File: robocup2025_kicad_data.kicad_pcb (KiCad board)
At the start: 2 copper layers, 11 parts, among them U1 RASPBERRY_PI_4B_4GB, U2 ESP32-DEVKITC-32E

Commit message: robocup2025_kicad_data.kicad_pcb,robocup2025_kicad_data.kicad_sch: Commit
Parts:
- U1: footprint robo:MODULE_RASPBERRY_PI_4B_4GB -> robo:raspberrypi5 small
- moved U1 19.0 mm to (136.1, 86.4)

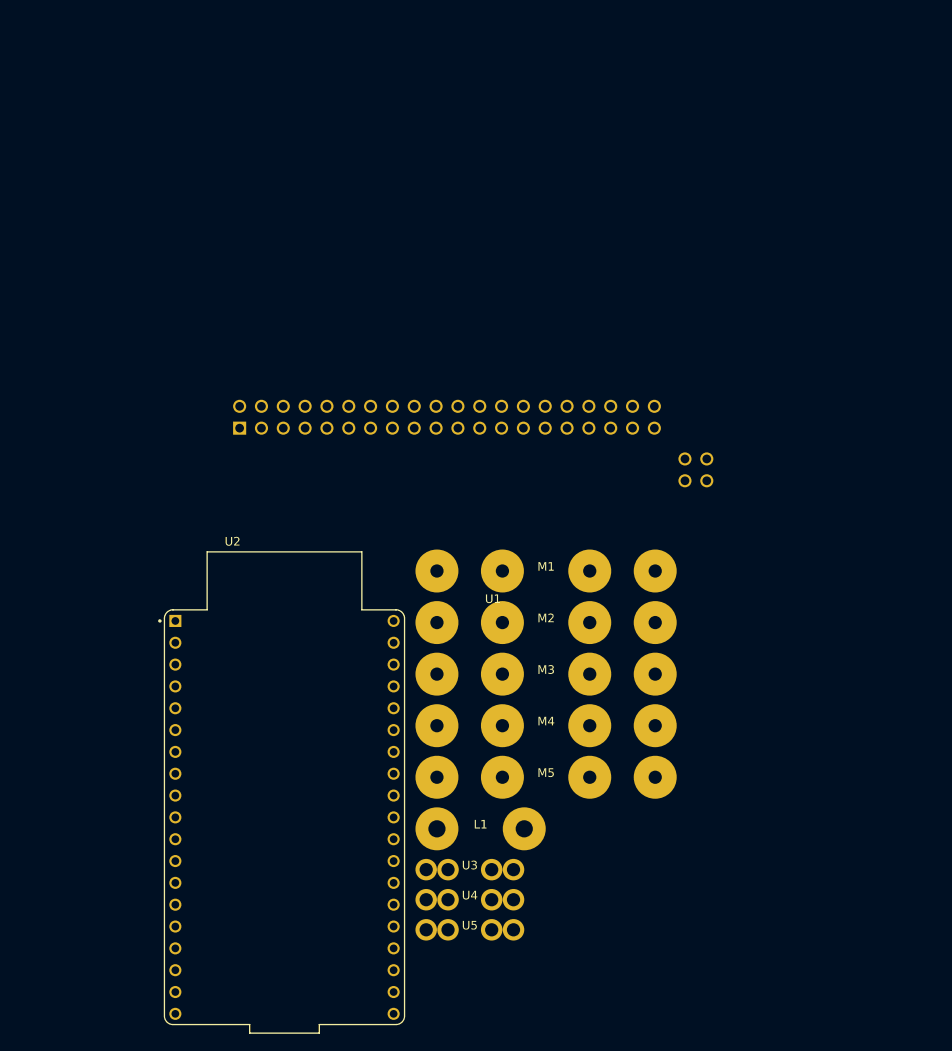
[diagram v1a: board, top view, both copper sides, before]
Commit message: robocup2025_kicad_data.kicad_pcb,robocup2025_kicad_data.kicad_prl: Replaced footprint, created cut layer
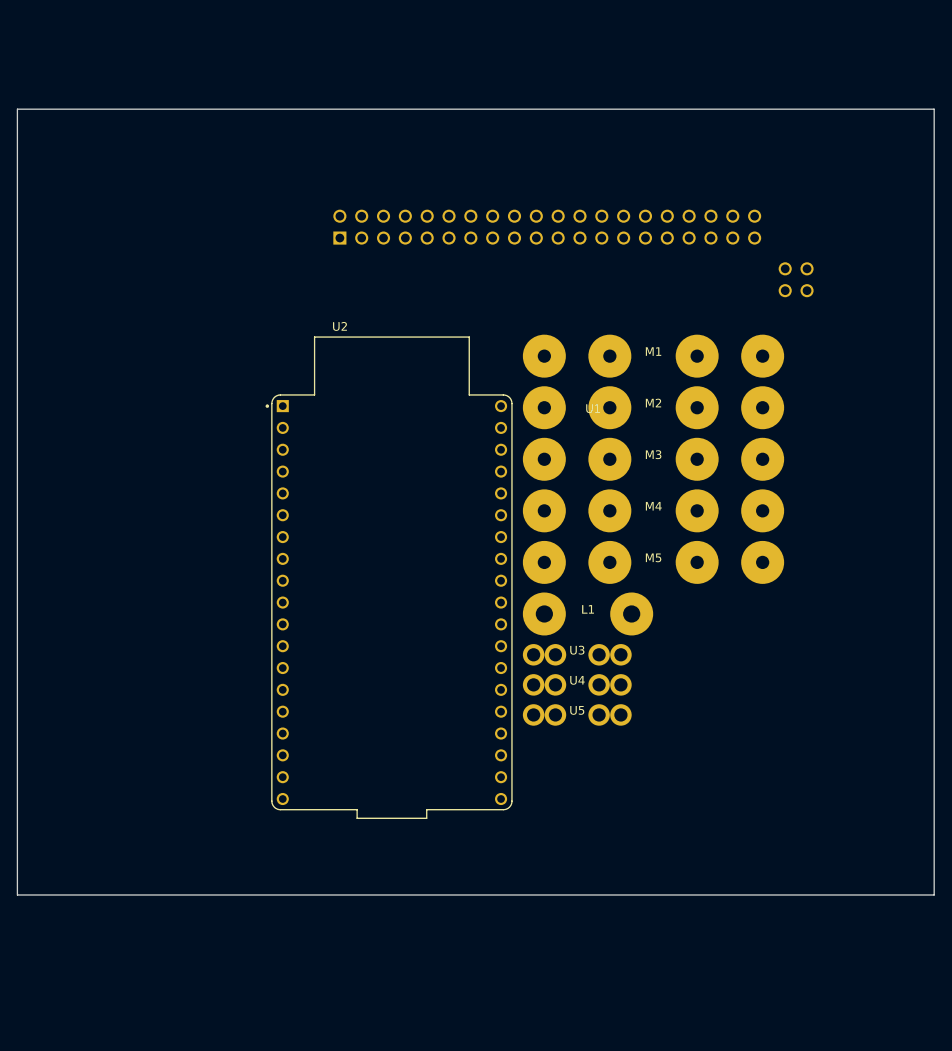
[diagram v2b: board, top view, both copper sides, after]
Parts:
- moved U2 28.0 mm to (124.9, 105.6)
- moved L1 28.0 mm to (147.7, 107.0)
- moved M1 28.0 mm to (155.3, 77.0)
- moved M2 28.0 mm to (155.3, 83.0)
- moved M3 28.0 mm to (155.3, 89.0)
- moved M4 28.0 mm to (155.3, 95.0)
- moved M5 28.0 mm to (155.3, 101.0)
- moved U3 28.0 mm to (146.4, 111.8)
- moved U4 28.0 mm to (146.4, 115.2)
- moved U5 28.0 mm to (146.4, 118.8)
- moved U1 25.0 mm to (147.8, 64.3)
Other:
- board outline added: 106.7 x 91.4 mm
- copper layers 2 -> 4

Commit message: robocup2025_kicad_data.kicad_pcb,robocup2025_kicad_data.kicad_prl robocup2025_kicad_data.kicad_pro: Set settings
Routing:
- added copper zone on B.Cu, net GND
- added copper zone on F.Cu, net LiPo+
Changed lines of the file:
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@@
 		(layer "Edge.Cuts")
+	)
+	(zone
+		(net 1)
+		(net_name "LiPo+")
+		(layer "F.Cu")
+		(hatch edge 0.5)
+		(connect_pads
+			(clearance 0.5)
+		)
+		(min_thickness 0.25)
+		(filled_areas_thickness no)
+		(fill yes
+			(thermal_gap 0.5)
+			(thermal_bridge_width 0.5)
+		)
+		(polygon
+			(pts
+				(xy 81.28 48.26) (xy 187.96 48.26) (xy 187.96 139.7) (xy 81.28 139.7)
+			)
+		)
+	)
+	(zone
+		(net 2)
+		(net_name "GND")
+		(layer "B.Cu")
+		(hatch edge 0.5)
+		(priority 1)
+		(connect_pads
+			(clearance 0.5)
+		)
+		(min_thickness 0.25)
+		(filled_areas_thickness no)
+		(fill yes
+			(thermal_gap 0.5)
+			(thermal_bridge_width 0.5)
+		)
+		(polygon
+			(pts
+				(xy 187.96 139.7) (xy 81.28 139.7) (xy 81.28 48.26) (xy 187.96 48.26)
+			)
+		)
 	)
 	(embedded_fonts no)

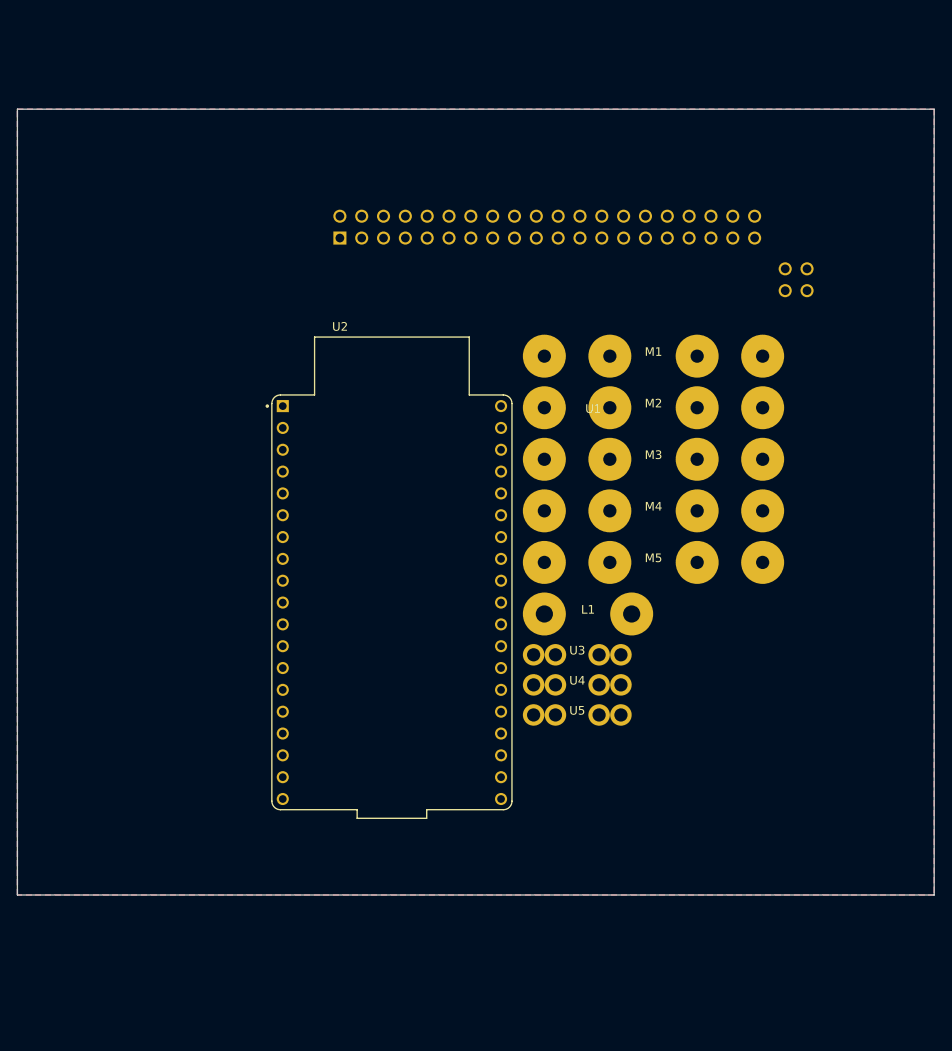
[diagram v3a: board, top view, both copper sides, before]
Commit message: robocup2025_kicad_data.kicad_pcb: Edited outline
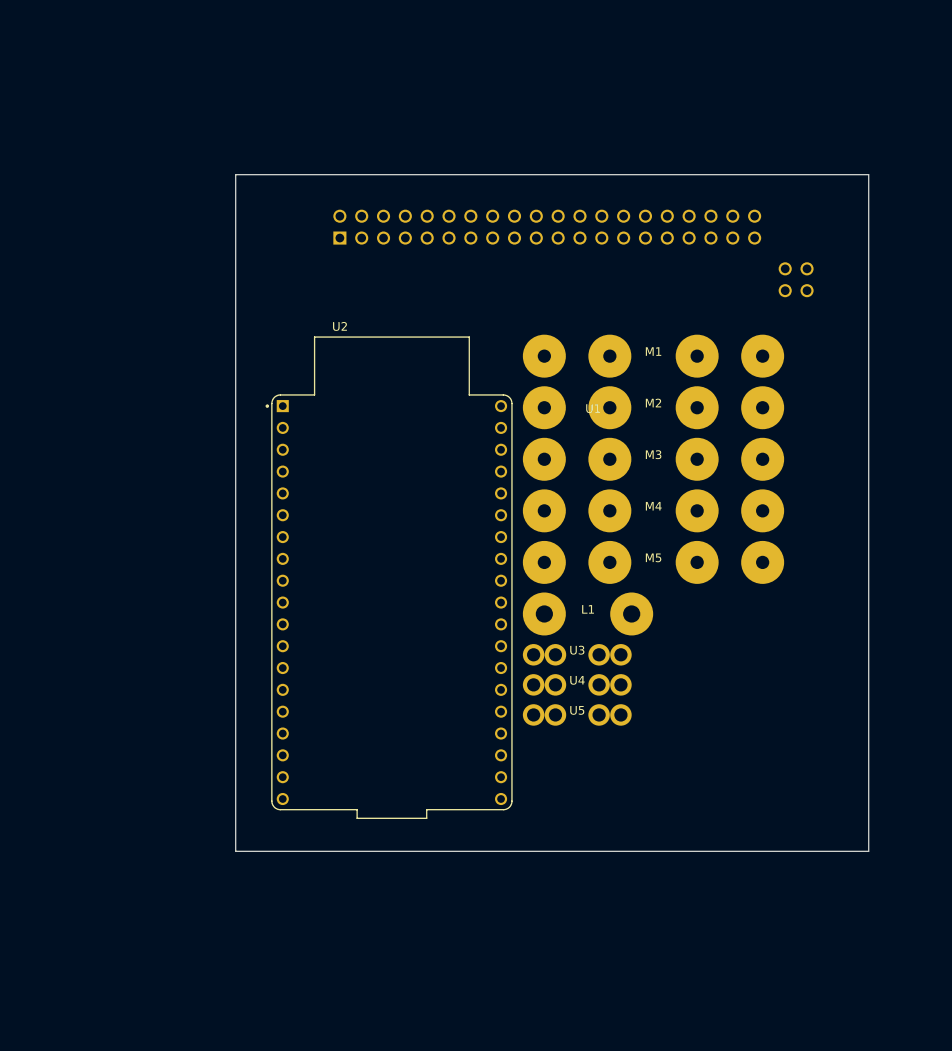
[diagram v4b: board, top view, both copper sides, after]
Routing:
- removed copper zone on B.Cu, net GND
- removed copper zone on F.Cu, net LiPo+
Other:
- board size 106.7 x 91.4 mm -> 73.7 x 78.7 mm
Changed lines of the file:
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@@
 	)
 	(gr_line
-		(start 81.28 48.26)
-		(end 81.28 139.7)
+		(start 106.68 55.88)
+		(end 106.68 134.62)
 		(stroke
 			(width 0.05)
@@
 	)
 	(gr_line
-		(start 187.96 48.26)
-		(end 187.96 139.7)
+		(start 180.34 55.88)
+		(end 180.34 134.62)
 		(stroke
 			(width 0.05)
@@
 	)
 	(gr_line
-		(start 81.28 48.26)
-		(end 187.96 48.26)
+		(start 106.68 55.88)
+		(end 180.34 55.88)
 		(stroke
 			(width 0.05)
@@
 	)
 	(gr_line
-		(start 81.28 139.7)
-		(end 187.96 139.7)
+		(start 106.68 134.62)
+		(end 180.34 134.62)
 		(stroke
 			(width 0.05)
@@
 		(layer "Edge.Cuts")
 	)
-	(zone
-		(net 1)
-		(net_name "LiPo+")
-		(layer "F.Cu")
-		(hatch edge 0.5)
-		(connect_pads
-			(clearance 0.5)
-		)
-		(min_thickness 0.25)
-		(filled_areas_thickness no)
-		(fill yes
-			(thermal_gap 0.5)
-			(thermal_bridge_width 0.5)
-		)
-		(polygon
-			(pts
-				(xy 81.28 48.26) (xy 187.96 48.26) (xy 187.96 139.7) (xy 81.28 139.7)
-			)
-		)
-	)
-	(zone
-		(net 2)
-		(net_name "GND")
-		(layer "B.Cu")
-		(hatch edge 0.5)
-		(priority 1)
-		(connect_pads
-			(clearance 0.5)
-		)
-		(min_thickness 0.25)
-		(filled_areas_thickness no)
-		(fill yes
-			(thermal_gap 0.5)
-			(thermal_bridge_width 0.5)
-		)
-		(polygon
-			(pts
-				(xy 187.96 139.7) (xy 81.28 139.7) (xy 81.28 48.26) (xy 187.96 48.26)
-			)
-		)
-	)
 	(embedded_fonts no)

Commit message: robocup2025_kicad_data.kicad_pcb,robocup2025_kicad_data.kicad_prl: Colored layer
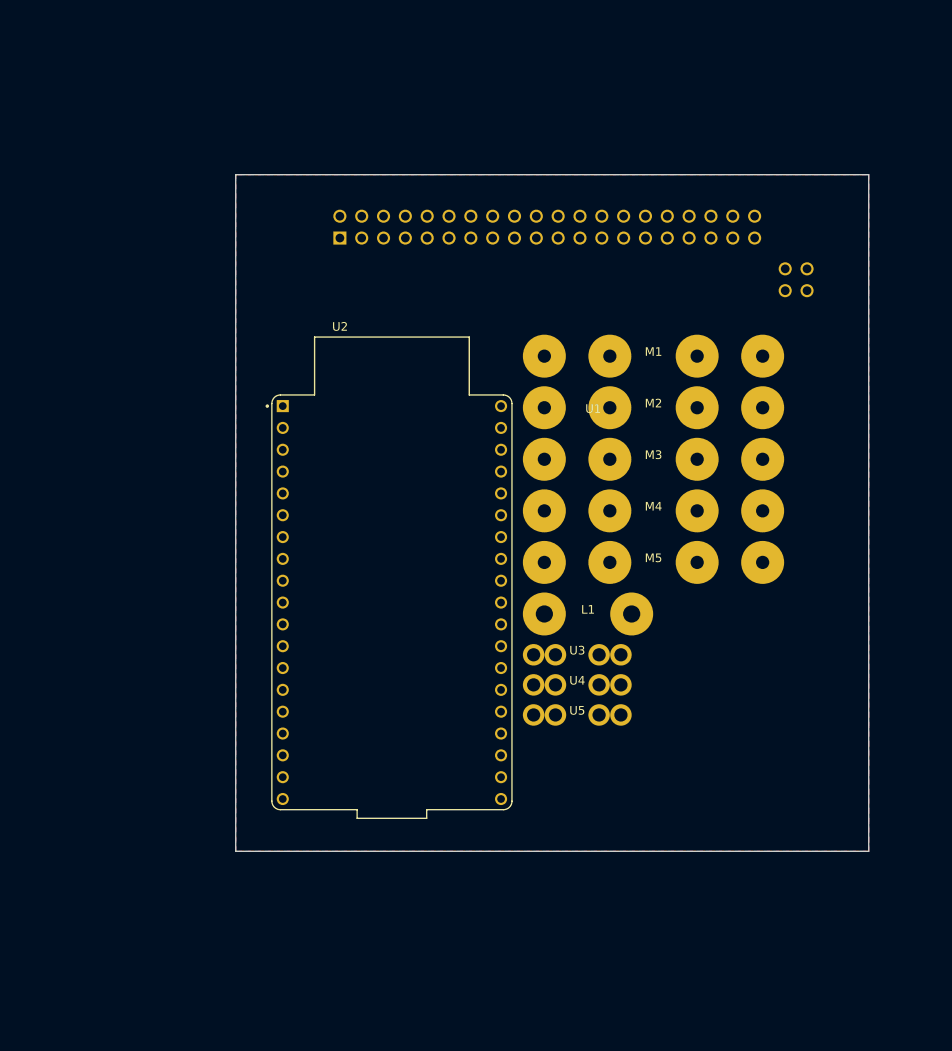
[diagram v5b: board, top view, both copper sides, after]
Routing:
- added copper zone on F.Cu, net GND
- added copper zone on B.Cu, net LiPo+
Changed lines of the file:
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@@
 		(layer "Edge.Cuts")
+	)
+	(zone
+		(net 2)
+		(net_name "GND")
+		(layer "F.Cu")
+		(hatch edge 0.5)
+		(connect_pads
+			(clearance 0.5)
+		)
+		(min_thickness 0.25)
+		(filled_areas_thickness no)
+		(fill yes
+			(thermal_gap 0.5)
+			(thermal_bridge_width 0.5)
+		)
+		(polygon
+			(pts
+				(xy 106.68 55.88) (xy 180.34 55.88) (xy 180.34 134.62) (xy 106.68 134.62)
+			)
+		)
+	)
+	(zone
+		(net 1)
+		(net_name "LiPo+")
+		(layer "B.Cu")
+		(hatch edge 0.5)
+		(priority 1)
+		(connect_pads
+			(clearance 0.5)
+		)
+		(min_thickness 0.25)
+		(filled_areas_thickness no)
+		(fill yes
+			(thermal_gap 0.5)
+			(thermal_bridge_width 0.5)
+		)
+		(polygon
+			(pts
+				(xy 180.34 55.88) (xy 106.68 55.88) (xy 106.68 134.62) (xy 180.34 134.62)
+			)
+		)
 	)
 	(embedded_fonts no)

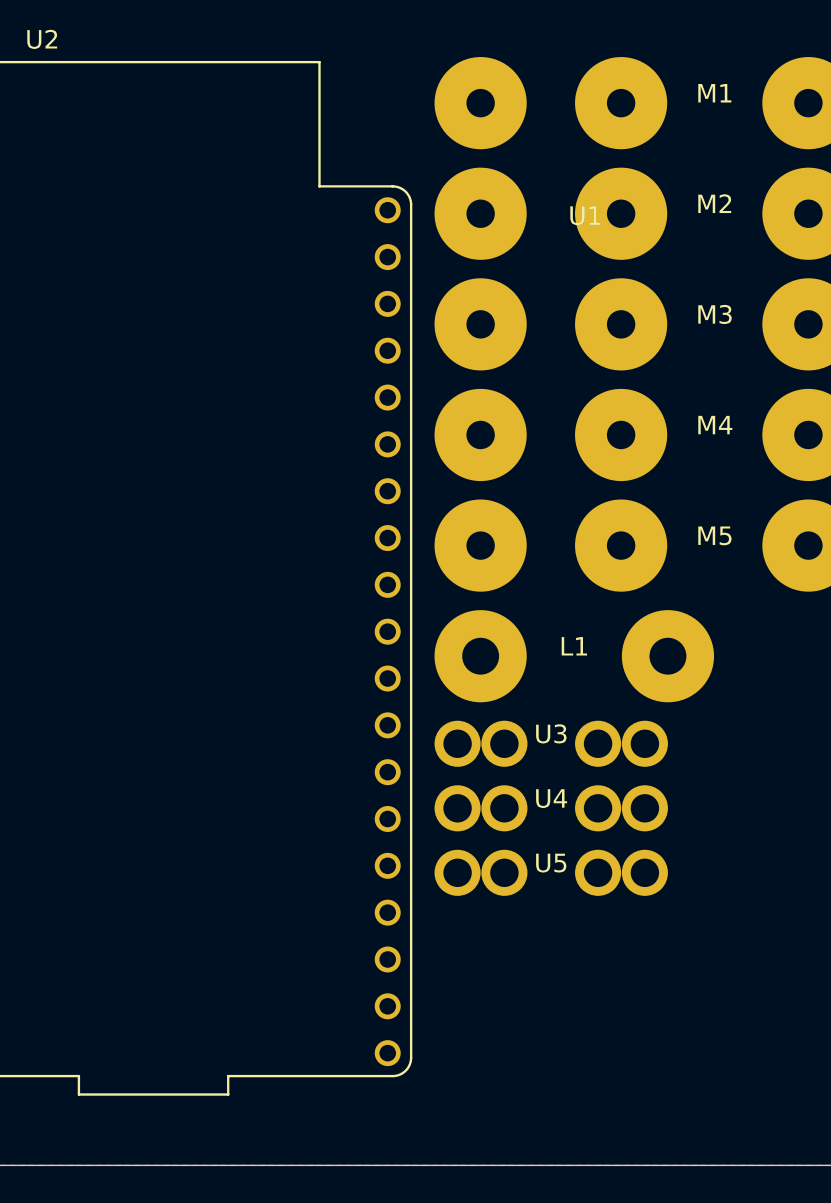
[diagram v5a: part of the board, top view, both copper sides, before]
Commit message: robocup2025_kicad_data.kicad_pcb,robocup2025_kicad_data.kicad_pro: Lined all the stuff
However, design check failing. The ultrasonic pads are causing the
trouble
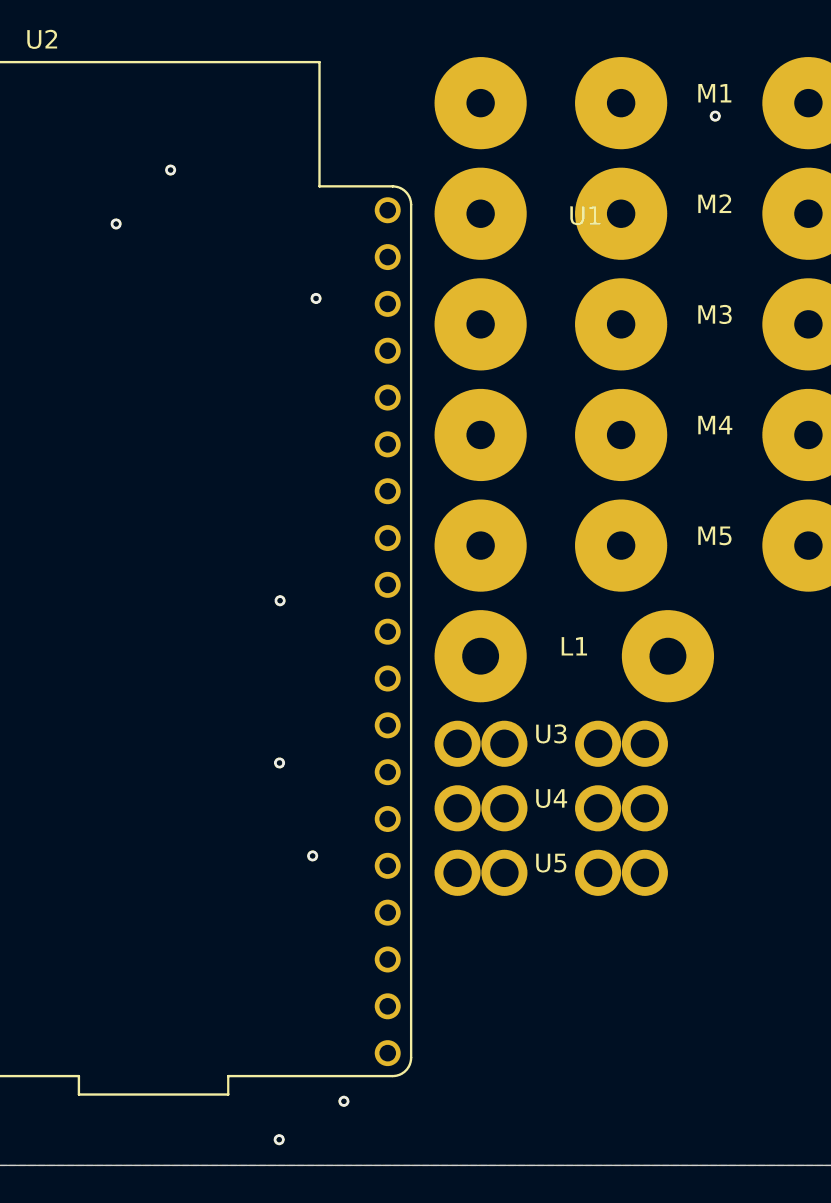
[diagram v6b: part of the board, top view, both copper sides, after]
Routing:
- net rasp_5V: track 0.00 -> 120.4 mm
- net ultrasonic_trig1: track 0.00 -> 102.6 mm
- net arm_feedback: track 0.00 -> 80.6 mm, vias 0 -> 1
- net ultrasonic_echo1: track 0.00 -> 70.2 mm, vias 0 -> 2
- net ultrasonic_echo3: track 0.00 -> 68.4 mm, vias 0 -> 1
- net tyre_pulse_1: track 0.00 -> 61.7 mm, vias 0 -> 1
- net ultrasonic_echo2: track 0.00 -> 60.5 mm
- net tyre_pulse_3: track 0.00 -> 54.9 mm, vias 0 -> 2
- net tyre_pulse_2: track 0.00 -> 53.9 mm, vias 0 -> 1
- net ultrasonic_trig3: track 0.00 -> 47.3 mm, vias 0 -> 1
- net ultrasonic_trig2: track 0.00 -> 45.1 mm
- net SDA: track 0.00 -> 39.0 mm
- net SCL: track 0.00 -> 30.3 mm
- net tyre_pulse_4: track 0.00 -> 17.8 mm
- net arm_pulse: track 0.00 -> 9.30 mm

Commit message: Save clear data Delete lines.
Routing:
- net rasp_5V: track 120.4 -> 0.00 mm
- net ultrasonic_trig1: track 102.6 -> 0.00 mm
- net arm_feedback: track 80.6 -> 0.00 mm, vias 1 -> 0
- net ultrasonic_echo1: track 70.2 -> 0.00 mm, vias 2 -> 0
- net ultrasonic_echo3: track 68.4 -> 0.00 mm, vias 1 -> 0
- net tyre_pulse_1: track 61.7 -> 0.00 mm, vias 1 -> 0
- net ultrasonic_echo2: track 60.5 -> 0.00 mm
- net tyre_pulse_3: track 54.9 -> 0.00 mm, vias 2 -> 0
- net tyre_pulse_2: track 53.9 -> 0.00 mm, vias 1 -> 0
- net ultrasonic_trig3: track 47.3 -> 0.00 mm, vias 1 -> 0
- net ultrasonic_trig2: track 45.1 -> 0.00 mm
- net SDA: track 39.0 -> 0.00 mm
- net SCL: track 30.3 -> 0.00 mm
- net tyre_pulse_4: track 17.8 -> 0.00 mm
- net arm_pulse: track 9.30 -> 0.00 mm
- removed copper zone on F.Cu, net GND
- removed copper zone on B.Cu, net LiPo+
